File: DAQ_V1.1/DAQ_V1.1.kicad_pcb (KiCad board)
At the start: 2 copper layers, 105.5 x 100 mm, 20 parts, among them J1 Screw_Terminal_01x02, J2 Screw_Terminal_01x04, J3 Screw_Terminal_01x04, J4 Screw_Terminal_01x04, J5 Screw_Terminal_01x04

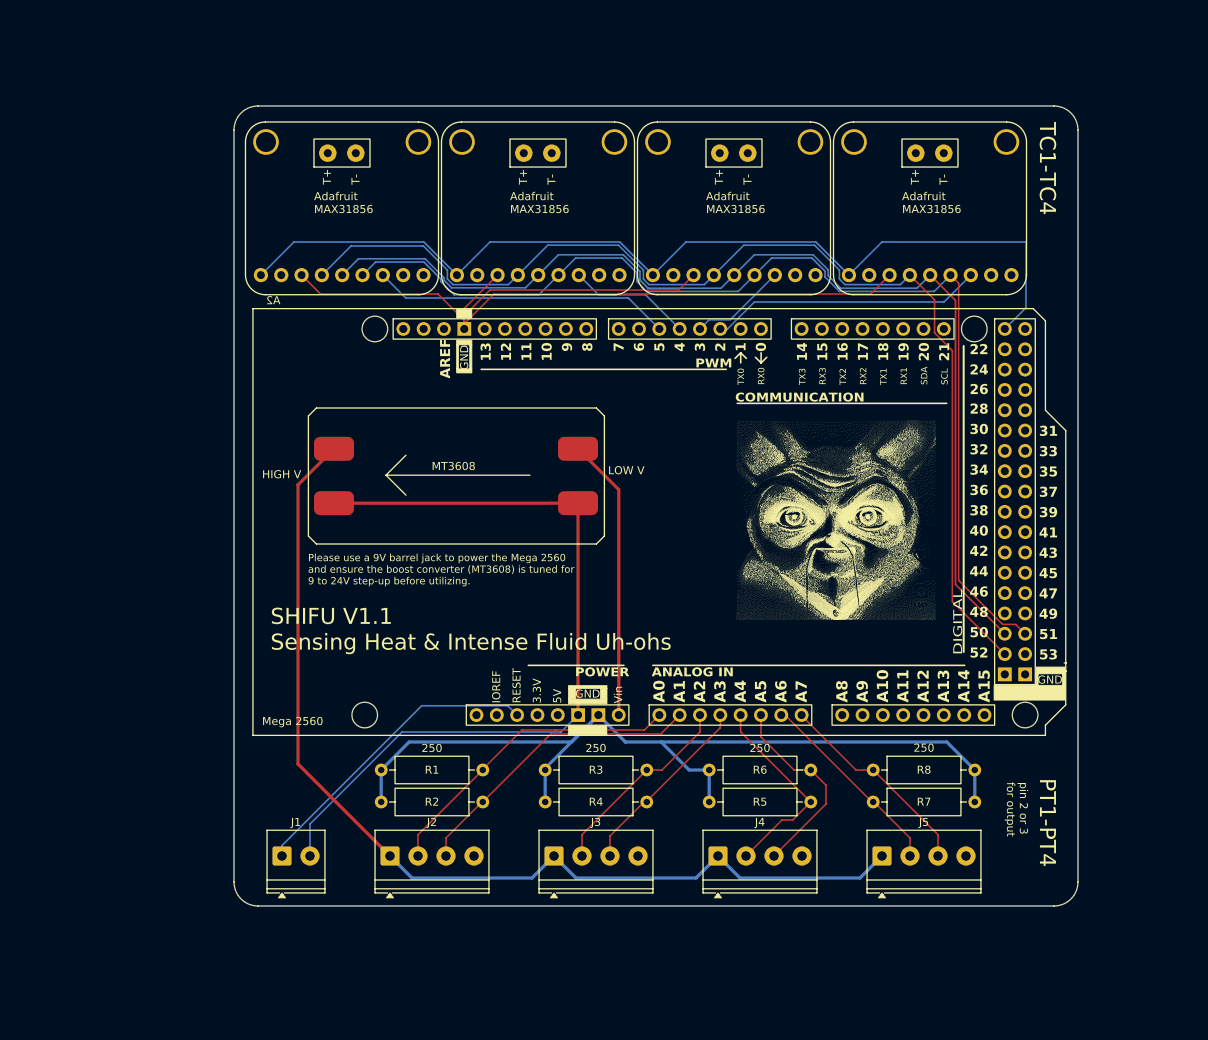
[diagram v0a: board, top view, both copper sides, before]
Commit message: Major changes to SHIFU PCB - Changed to 4 layer - Added Ground Planes - Filled Zones - Pi filter integration
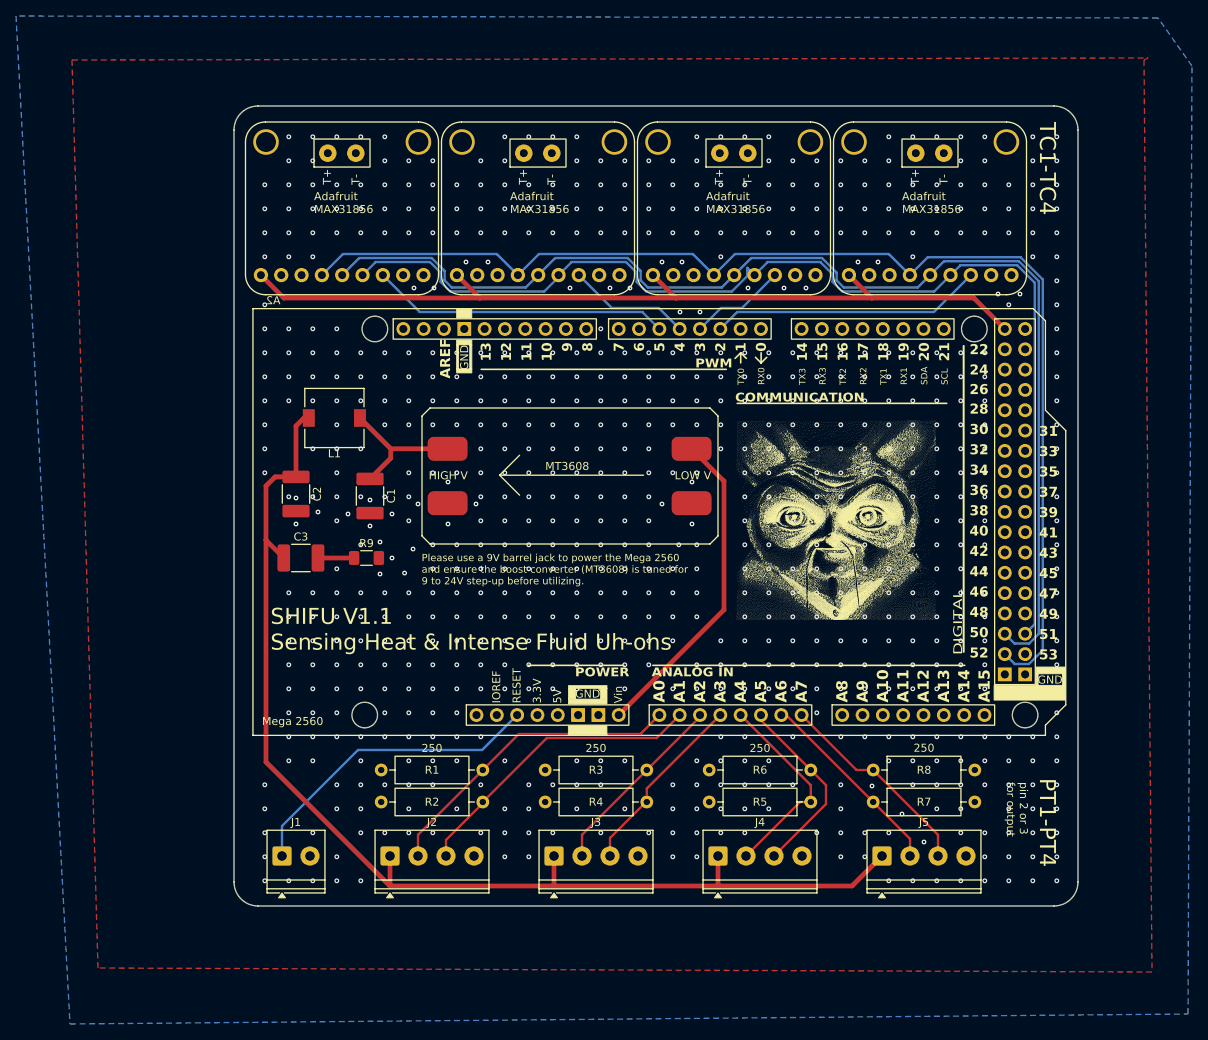
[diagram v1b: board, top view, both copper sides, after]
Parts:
- added C1: 22u, Capacitor_SMD:C_1812_4532Metric_Pad1.57x3.40mm_HandSolder, F.Cu at (102.5, 87.2)
- added C2: 10u, Capacitor_SMD:C_1812_4532Metric_Pad1.57x3.40mm_HandSolder, F.Cu at (93.2, 87.0)
- added C3: 47u, Capacitor_SMD:C_1812_4532Metric_Pad1.57x3.40mm_HandSolder, F.Cu at (93.9, 95.0)
- added L1: 10u, Inductor_SMD:L_7.3x7.3_H3.5, F.Cu at (98.0, 77.5)
- added R9: R, Resistor_SMD:R_1206_3216Metric_Pad1.30x1.75mm_HandSolder, F.Cu at (102.1, 95.0)
- moved U5 14.2 mm to (127.7, 84.2)
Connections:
- A2 pad GND2: GND2 -> GND
- A2 pad GND3: GND3 -> GND
- J1 pad 2: GND2 -> GND
- R1 pad 2: GND3 -> GND
- R2 pad 2: GND3 -> GND
- R3 pad 2: GND3 -> GND
- R4 pad 2: GND3 -> GND
- R5 pad 2: GND3 -> GND
- R6 pad 2: GND3 -> GND
- R7 pad 2: GND3 -> GND
- R8 pad 2: GND3 -> GND
- U5 pad 2: GND2 -> GND
- U5 pad 3: Net-(J2-Pin_1) -> Net-(U5-Vout+)
- U5 pad 4: GND2 -> GND
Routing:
- net GND: track 121.0 -> 0.00 mm, vias 0 -> 777
- net GND3: track 113.1 -> 0.00 mm
- net GND2: track 100.1 -> 0.00 mm
- net Net-(J2-Pin_1): track 125.9 -> 146.5 mm
- net Net-(U5-Vout+): track 0.00 -> 17.4 mm
- net Net-(A2-D50_MISO): track 133.4 -> 149.2 mm
- net Net-(U1-Vin): track 119.6 -> 107.9 mm
- net Net-(A2-D52_SCK): track 139.9 -> 151.1 mm
- net Net-(A2-D51_MOSI): track 134.7 -> 142.4 mm
- net Net-(U5-Vin+): track 35.4 -> 40.4 mm
- net Net-(C3-Pad2): track 0.00 -> 4.51 mm
- net Net-(J4-Pin_3): track 24.9 -> 23.7 mm
- net Net-(J3-Pin_2): track 24.8 -> 23.7 mm
- added copper zone on B.Cu, net GND
- added copper zone on F.Cu, net GND
- added copper zone on In1.Cu, net GND
- added copper zone on In2.Cu, net GND
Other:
- copper layers 2 -> 4
